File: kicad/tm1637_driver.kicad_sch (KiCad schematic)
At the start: 11 parts, among them U2 TM1637

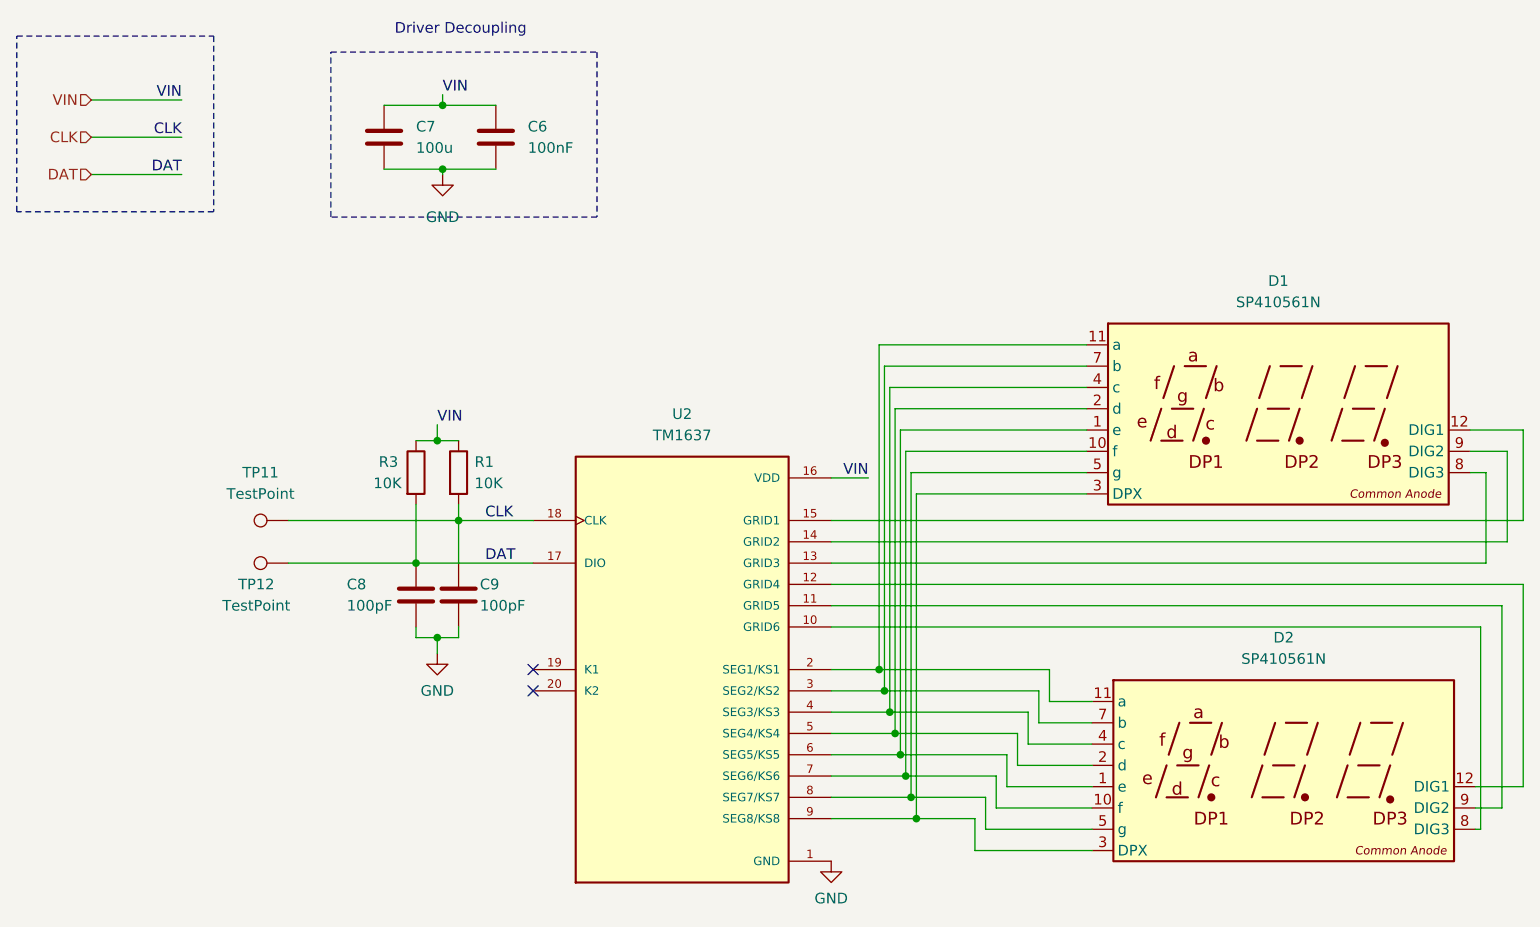
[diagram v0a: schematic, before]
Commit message: adding v-alpha prototype gerbers (note out of sync with kicad files)
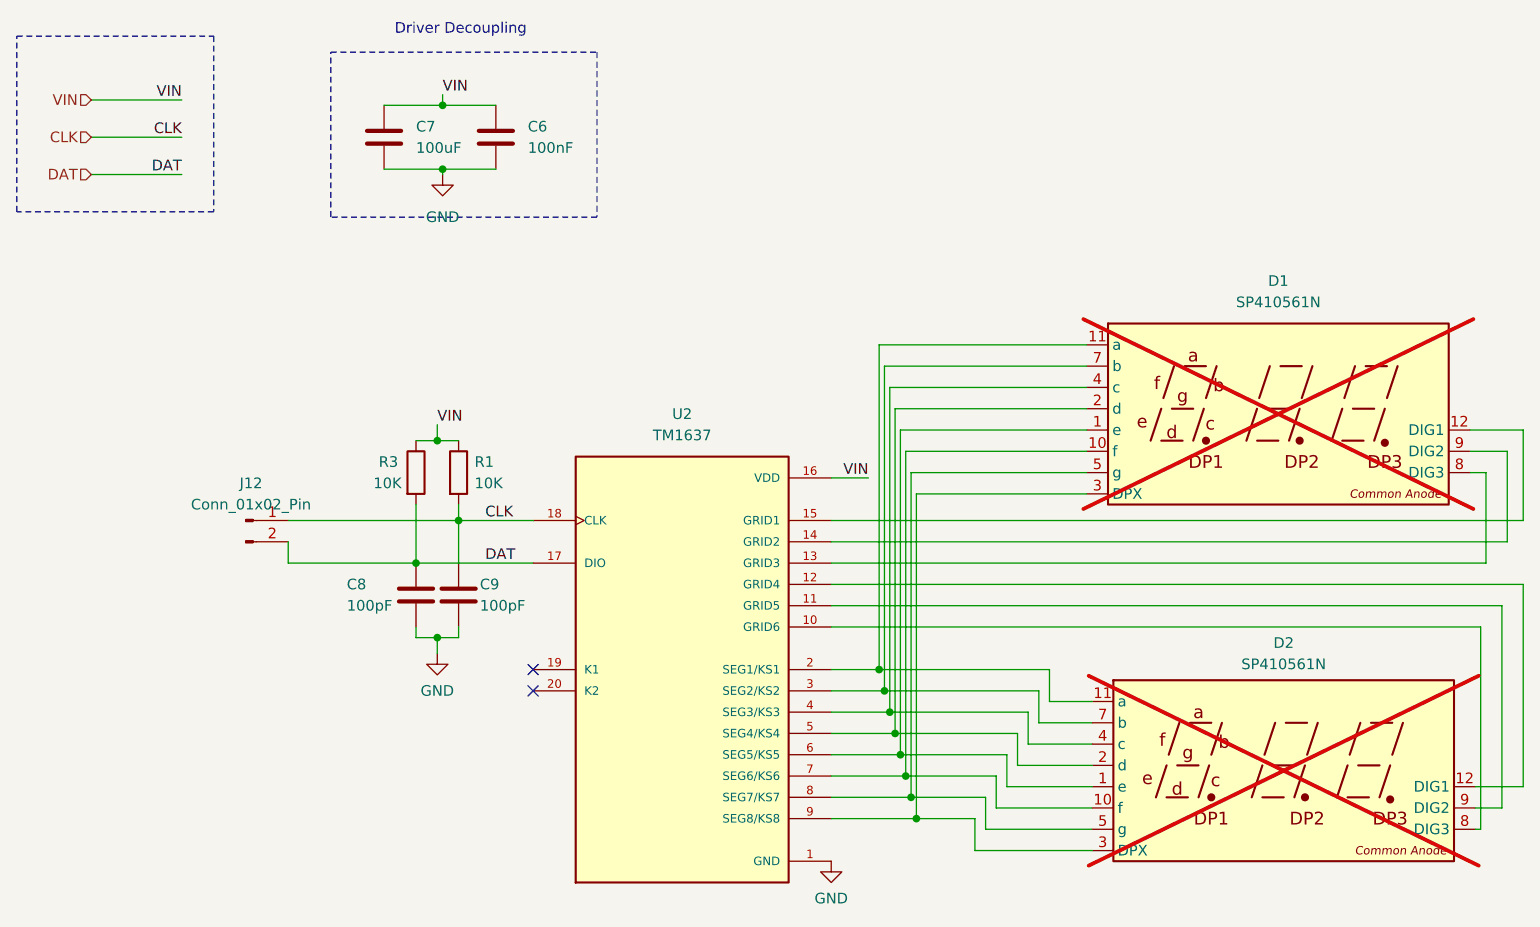
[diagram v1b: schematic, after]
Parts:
- removed TP11, TP12: TestPoint, symbol Connector:TestPoint
- added J12: Conn_01x02_Pin, Connector_PinHeader_2.54mm:PinHeader_1x02_P2.54mm_Vertical, symbol Connector:Conn_01x02_Pin
- C6: footprint Capacitor_SMD:C_0805_2012Metric -> Capacitor_SMD:C_0603_1608Metric; Basic/Extended (none) -> Basic; DOUBLE_CHECK (none) -> x; JLPCB_MPN (none) -> CC0603KRX7R9BB104; JLPCB_Mfg (none) -> YAGEO; JLPCB_Part_No (none) -> C14663; JLPCB_Price (none) -> 0.0021; JLPCB_URL (none) -> https://jlcpcb.com/partdetail/Yageo-CC0603KRX7R9BB104/C14663; LCSC Part # (none) -> C14663
- C7: value 100u -> 100uF; footprint Capacitor_SMD:C_0805_2012Metric -> Capacitor_SMD:C_1206_3216Metric; Basic/Extended (none) -> Basic; DOUBLE_CHECK (none) -> x; JLPCB_MPN (none) -> CL31A107MQHNNNE; JLPCB_Mfg (none) -> Samsung Electro-Mechanics; JLPCB_Part_No (none) -> C15008; JLPCB_URL (none) -> https://jlcpcb.com/partdetail/15681-CL31A107MQHNNNE/C15008; LCSC Part # (none) -> C15008
- C8, C9: footprint Capacitor_SMD:C_0805_2012Metric -> Capacitor_SMD:C_0603_1608Metric; Basic/Extended (none) -> Basic; DOUBLE_CHECK (none) -> x; JLPCB_MPN (none) -> CL10C101JB8NNNC; JLPCB_Mfg (none) -> Samsung Electro-Mechanics; JLPCB_Part_No (none) -> C14858; JLPCB_URL (none) -> https://jlcpcb.com/partdetail/15530-CL10C101JB8NNNC/C14858; LCSC Part # (none) -> C14858
- D1, D2: Basic/Extended (none) -> Extended; DNP (none) -> DNP; JLPCB_MPN (none) -> SP410561N; JLPCB_Mfg (none) -> ARKLED(Wuxi ARK Tech Elec); JLPCB_Part_No (none) -> C98924; JLPCB_Price (none) -> 0.3780; JLPCB_URL (none) -> https://jlcpcb.com/partdetail/arkled_wuxi_Ark_Tech_elec-SP4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; LCSC Part # (none) -> C98924; now not fitted; now left out of the parts list
- R1, R3: footprint Resistor_SMD:R_0805_2012Metric -> Resistor_SMD:R_0603_1608Metric; Basic/Extended (none) -> Basic; JLPCB_MPN (none) -> 0603WAF1002T5E; JLPCB_Mfg (none) -> UNI-ROYAL(Uniroyal Elec); JLPCB_Part_No (none) -> C25804; JLPCB_URL (none) -> https://jlcpcb.com/partdetail/26547-0603WAF1002T5E/C25804; LCSC Part # (none) -> C25804
- U2: footprint 01-User-Footprints:TM_TM1637(TA2007)_SOC20 -> 01-User-Footprints:TM_TM1637(TA2007)_SOC-20_12.6x7.5_P1.27_PD0.44x2; Basic/Extended (none) -> Extended; DOUBLE_CHECK x -> done; JLPCB_MPN (none) -> TM1637(TA2007); JLPCB_Part_No (none) -> C5337160; JLPCB_Price (none) -> 0.1674; JLPCB_URL (none) -> https://jlcpcb.com/partdetail/6103284-TM1637_TA2007/C5337160; LCSC Part # (none) -> C5337160
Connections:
- net CLK: now also J12.1 (Pin_1)
- net DAT: now also J12.2 (Pin_2)
